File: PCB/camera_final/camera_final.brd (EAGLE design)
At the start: 61.5 x 35.4 mm, 16 parts

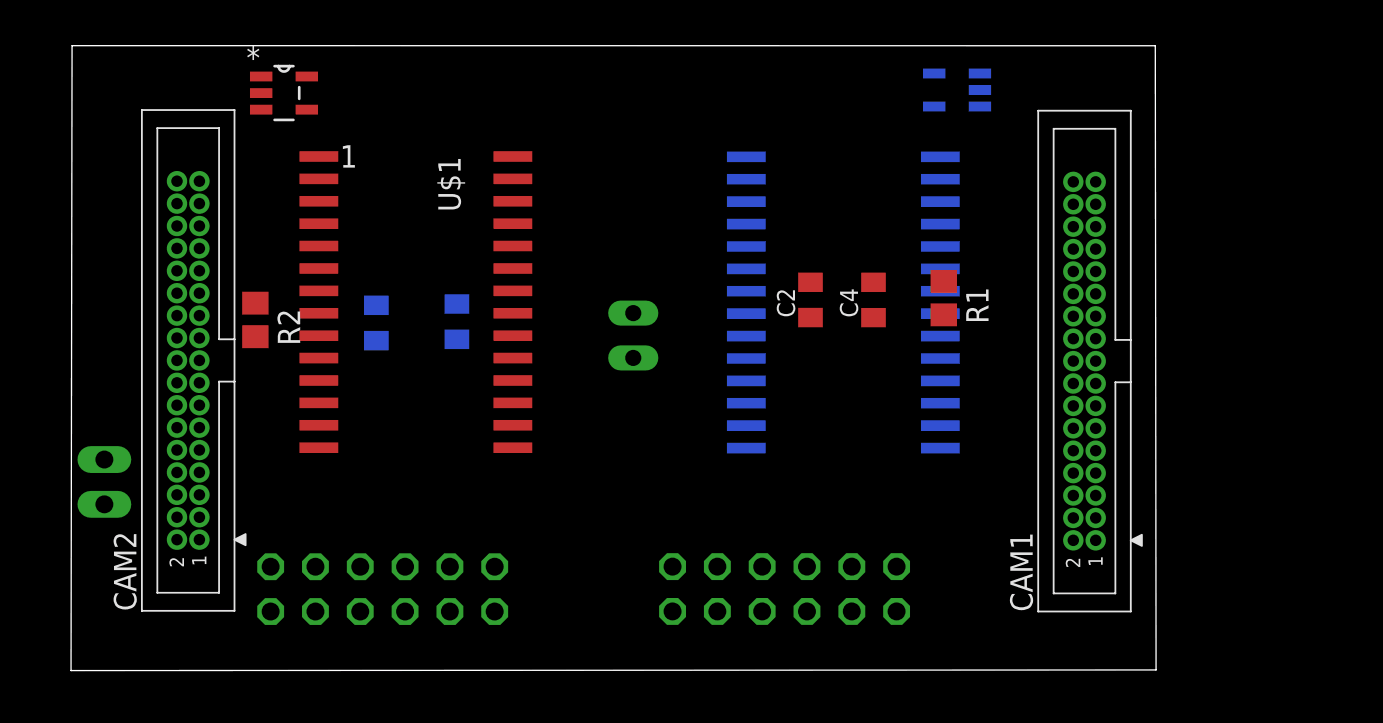
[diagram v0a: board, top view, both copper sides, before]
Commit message: routing stereo camera board
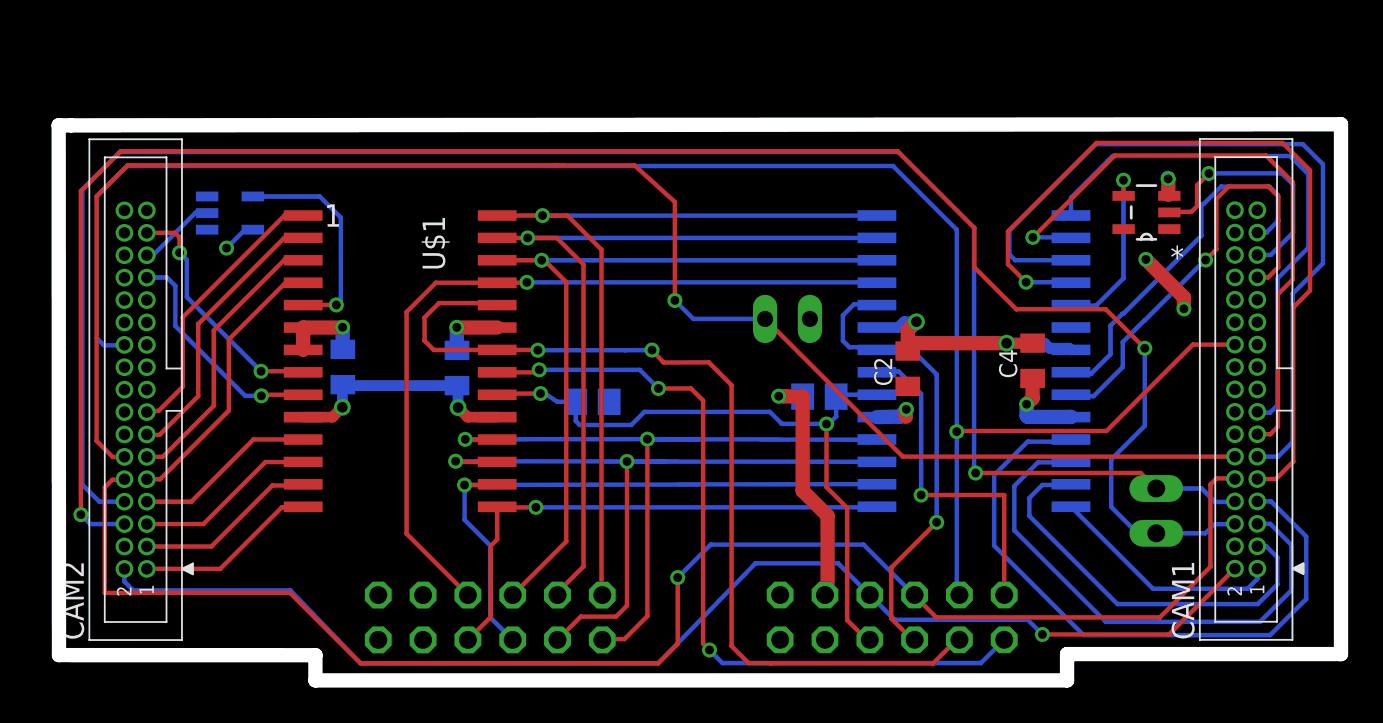
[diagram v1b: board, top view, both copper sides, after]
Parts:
- moved I2C 59.7 mm to (61.6, 9.51)
- moved R2 19.7 mm to (29.7, 15.7), flipped to the bottom, turned to 0 degrees
- moved INV1 12.8 mm to (61.1, 26.4), flipped to the top, turned to 180 degrees
- moved C4 9.66 mm to (54.6, 18.0)
- moved CAM1 9.30 mm to (66.7, 16.4)
- moved R1 8.99 mm to (42.5, 16.0), flipped to the bottom, turned to 180 degrees
- moved CAM_OE 8.79 mm to (40.7, 20.4), turned to 90 degrees
- moved U$2 8.12 mm to (51.3, 18.0)
- moved INV2 7.46 mm to (9.12, 26.4), flipped to the bottom, turned to 180 degrees
- moved C2 6.75 mm to (47.5, 17.6)
- moved PMODA 6.31 mm to (46.7, 3.48)
- moved PMODB 6.31 mm to (23.9, 3.47)
- moved U$1 3.47 mm to (18.8, 18.0)
- moved CAM2 3.41 mm to (3.78, 16.4)
- moved C1 3.14 mm to (15.5, 17.7)
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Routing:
- net SDA: track 0.00 -> 105.8 mm, vias 0 -> 2
- net SCL: track 0.00 -> 102.1 mm, vias 0 -> 1
- net TRIG: track 0.00 -> 99.3 mm, vias 0 -> 1
- net OE: track 0.00 -> 91.2 mm, vias 0 -> 1
- net /RST: track 0.00 -> 85.7 mm, vias 0 -> 1
- net SCLK: track 0.00 -> 71.3 mm, vias 0 -> 1
- net RE2: track 0.00 -> 53.0 mm, vias 0 -> 2
- net D0: track 0.00 -> 45.3 mm, vias 0 -> 1
- net C1D5: track 0.00 -> 45.1 mm, vias 0 -> 1
- net D3: track 0.00 -> 44.9 mm, vias 0 -> 1
- net D1: track 0.00 -> 44.7 mm, vias 0 -> 1
- net RRST2: track 0.00 -> 44.3 mm, vias 0 -> 3
- net C1D4: track 0.00 -> 44.2 mm
- net D2: track 0.00 -> 42.4 mm, vias 0 -> 1
- net D5: track 0.00 -> 41.4 mm, vias 0 -> 2
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- added copper zone on layer 1, net 3V3
- added copper zone on layer 16, net GND
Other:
- board size 61.5 x 35.4 mm -> 72.7 x 31.5 mm

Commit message: semi-finalized layout
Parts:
- removed R2: (no value), rcl:R0805
- moved R1 8.76 mm to (43.9, 7.34), flipped to the top, turned to 0 degrees
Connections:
- net GND: no longer R2.1
- net RCK: no longer R2.2
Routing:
- net GND: track 41.1 -> 49.3 mm, vias 8 -> 12
- net RRST2: track 44.3 -> 45.8 mm
- net RCK: track 38.2 -> 36.9 mm
- net /RST: track 85.7 -> 86.8 mm
- net SDA: track 105.8 -> 106.4 mm
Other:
- board size 72.7 x 31.5 mm -> 73.6 x 31.5 mm
- board text added: "2016 WPI MQP"
- board text added: "AL422b"
- board text added: "Control"
- board text added: "Data"
- board text added: "Georges Gauthier & John DeCusati"
- board text added: "I2C"
- board text added: "MT9V034 PMOD Stereo Camera Breakout"
- board text added: "mm baseline"

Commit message: ordered the board!
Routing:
- net TRIG: track 99.3 -> 102.7 mm
- net RRST1: track 19.2 -> 17.3 mm
- net C1D9: track 13.3 -> 14.2 mm
- net SDA: track 106.4 -> 107.1 mm
- net C1D5: track 45.1 -> 44.5 mm
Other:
- board text added: "SCL"
- board text added: "SDA"
